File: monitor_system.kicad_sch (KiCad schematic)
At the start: 2 parts, among them K1 DIPxx-1Axx-11x, U1 ACS781xLRTR-050B

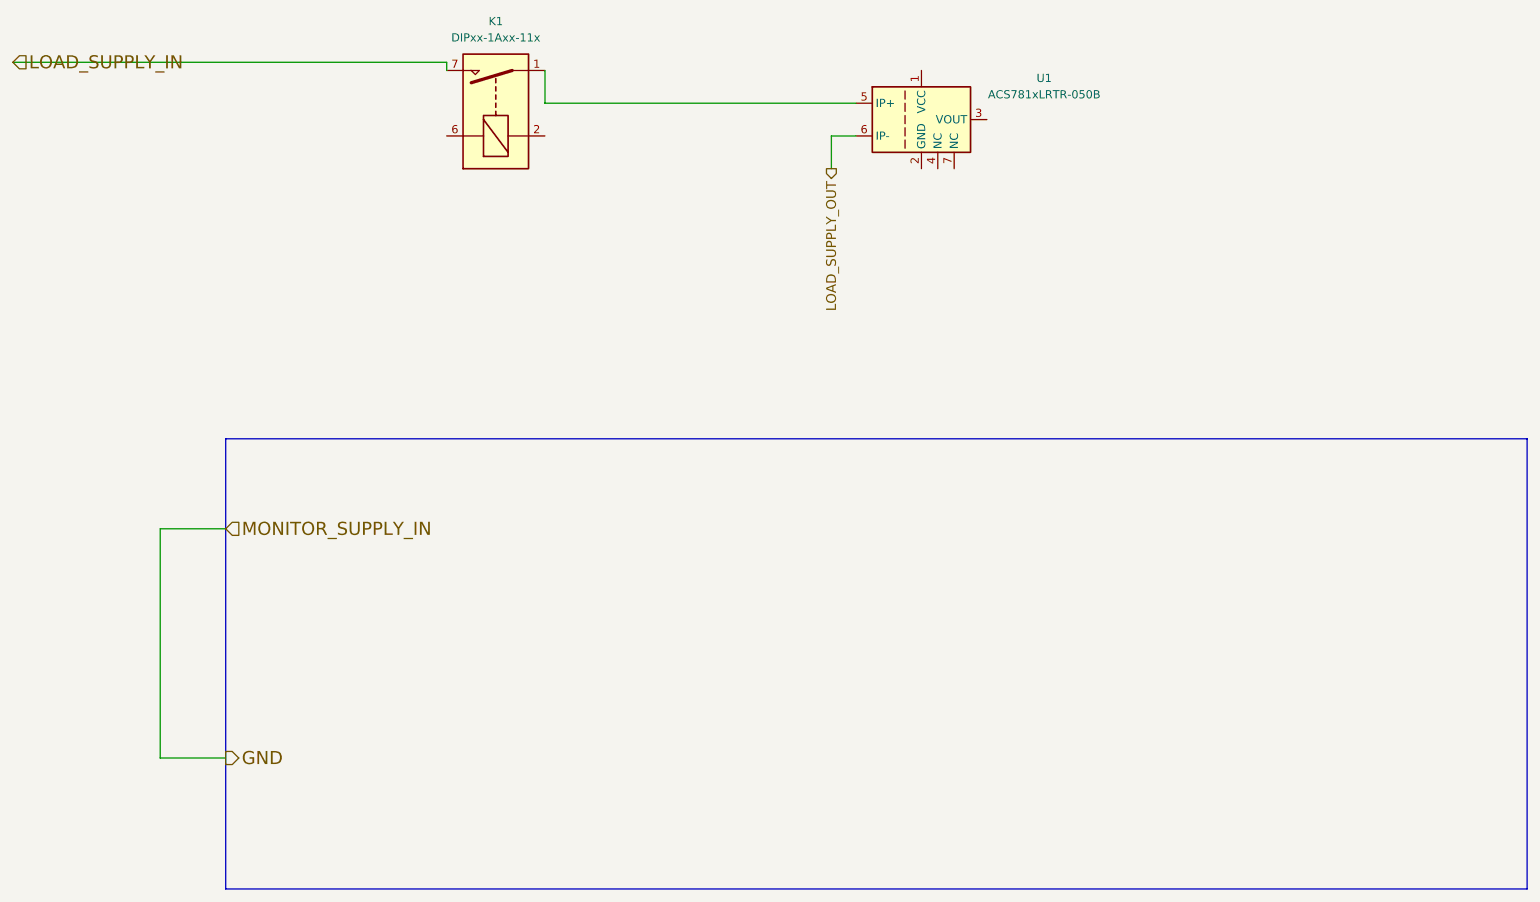
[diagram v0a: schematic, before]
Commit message: feat:added default kicad .gitignore from:https://github.com/github/gitignore/blob/master/KiCad.gitignore
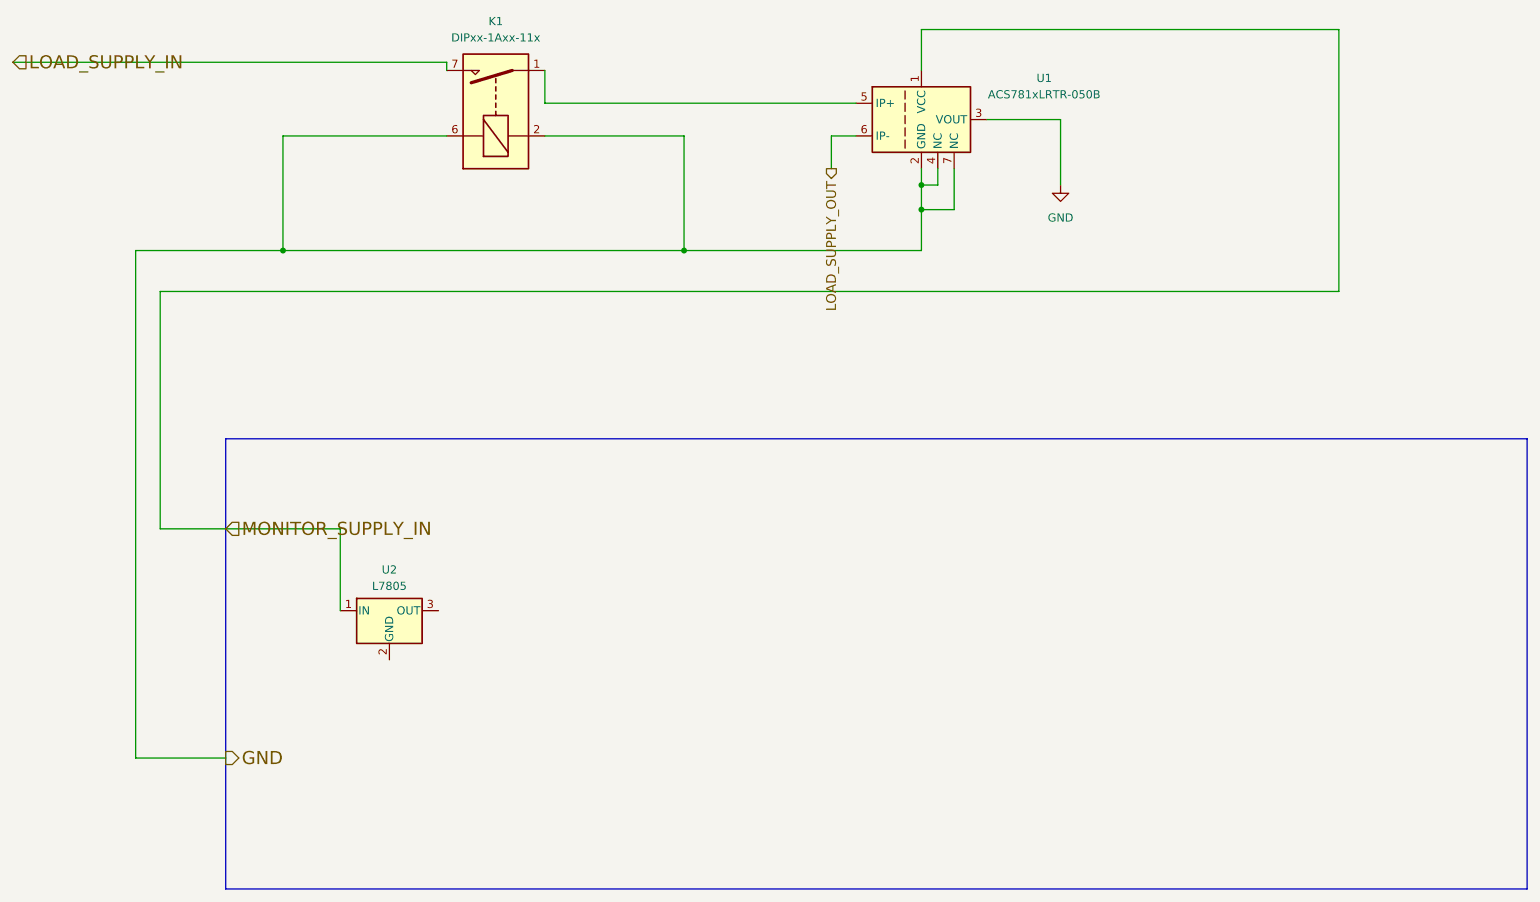
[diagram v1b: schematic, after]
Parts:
- added U2: L7805, symbol Regulator_Linear:L7805
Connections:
- net GND: now also K1.2, K1.6, U1.2 (GND), U1.3 (VOUT), U1.4 (NC), U1.7 (NC)
- net MONITOR_SUPPLY_IN: now reaches U1.1 (VCC)
- net MONITOR_SUPPLY_IN: now also U2.1 (IN)
